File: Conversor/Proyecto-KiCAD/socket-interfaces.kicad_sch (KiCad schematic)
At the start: 37 parts

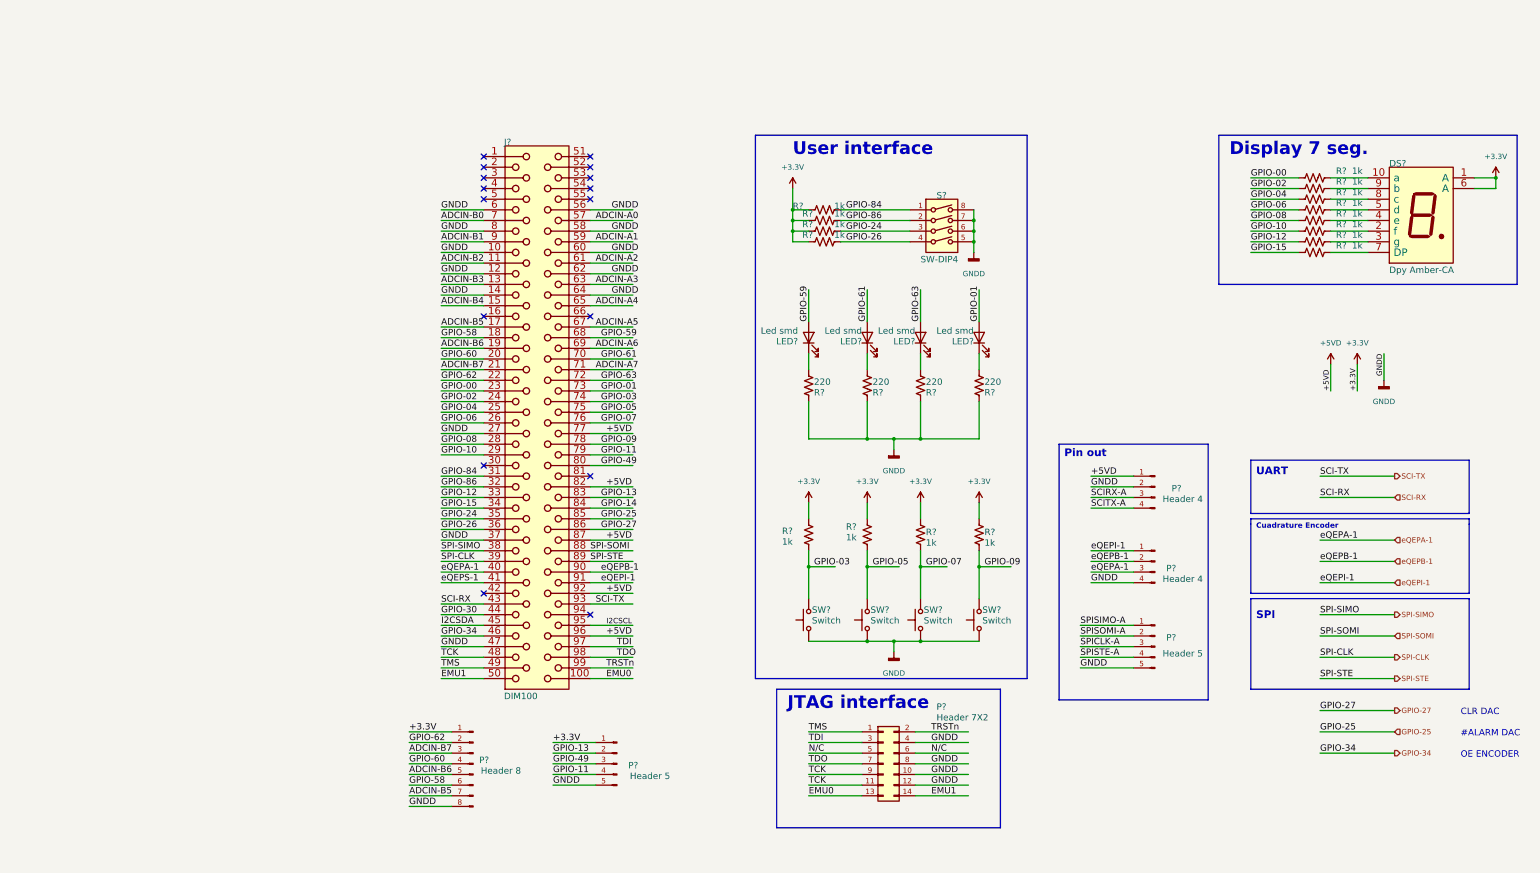
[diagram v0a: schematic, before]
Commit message: Seleccionar componentes de los que me dieron y seguir con la placa adaptadora
- OpAmp OPA365AID para acondicionamiento de señales del sensor de efecto
hall
- Los optos que hay son ACPL-P343 en vez de P480, que necesitan 15-30V
de alimentación. Preguntar si no es mejor cambiarlos por 6N137, de 5V de
Vcc
- Regulador solo hay LM7805 de 5Vout pero también necesito 3.3Vout
- No hay ningún diodo en las cosas que me dieron

Por hacer:
  - Preguntar por los 6N137 y algun regulador de 3V3 out
  - Preguntar por los diodos del puente del conversor
  - Terminar de pasar la placa adaptadora del DSP
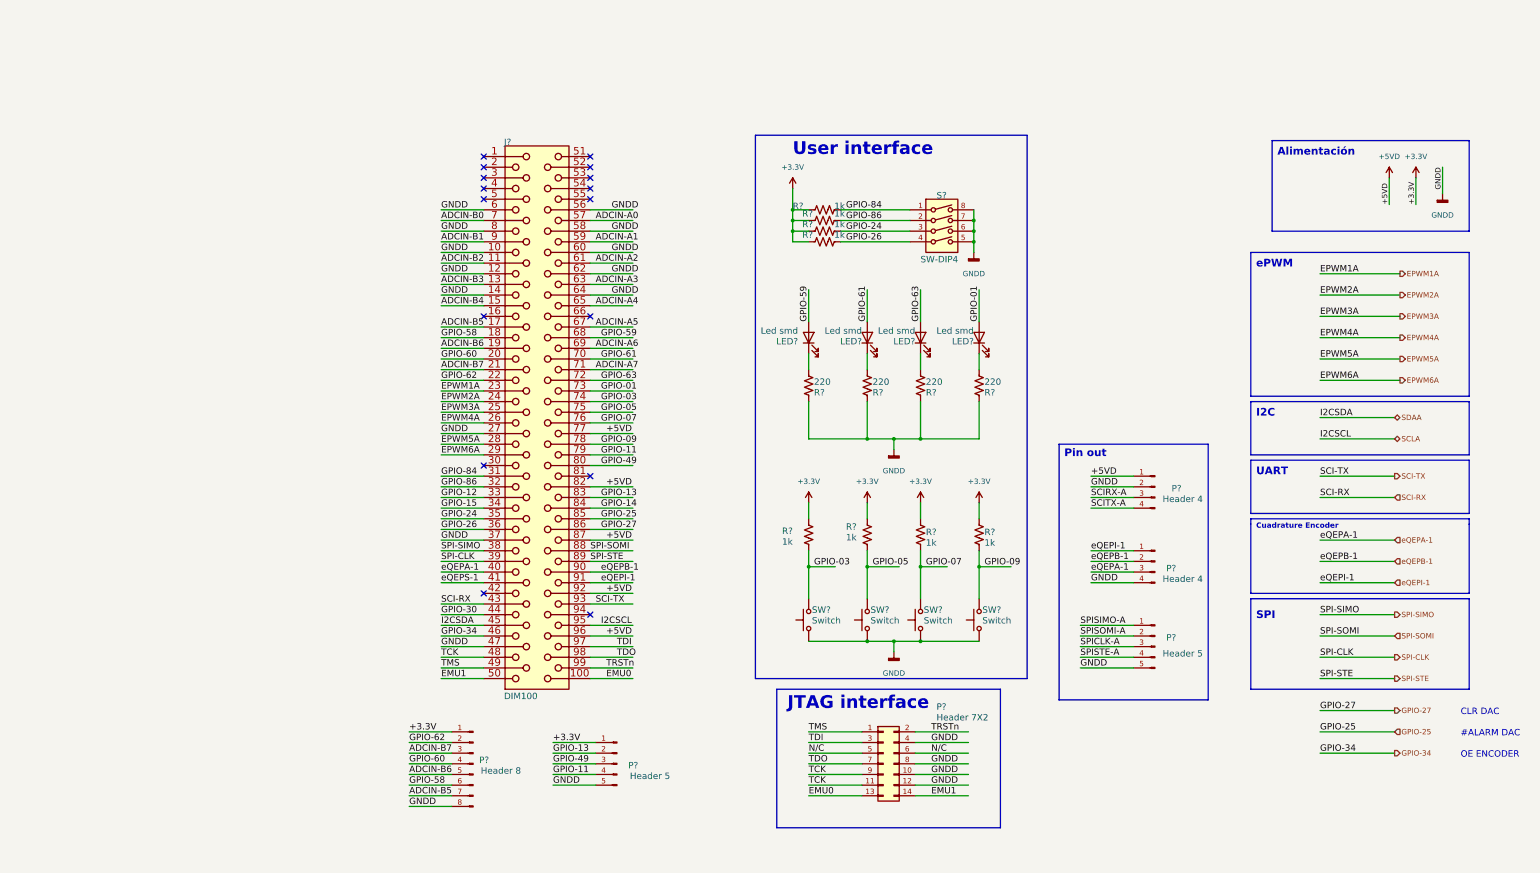
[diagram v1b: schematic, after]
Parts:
- removed DS?: Dpy Amber-CA, symbol dpy_amber-ca:Dpy_Amber-CA-
- removed R? (x8): 1k, symbol Device:R_US
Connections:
- net GPIO-00 renamed EPWM1A
- net GPIO-02 renamed EPWM2A
- net GPIO-04 renamed EPWM3A
- net GPIO-06 renamed EPWM4A
- net GPIO-08 renamed EPWM5A
- net GPIO-10 renamed EPWM6A
- net I2CSCL renamed SCLA
- net I2CSDA renamed SDAA
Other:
- note added: "Alimentación"
- note added: "I2C"
- note added: "ePWM"
- note removed: "Display 7 seg."

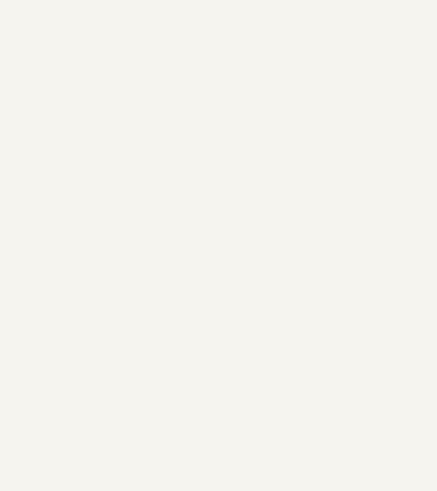
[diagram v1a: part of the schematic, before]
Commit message: Agregar simbolo, footprint y modelo 3D del slot DIMM100
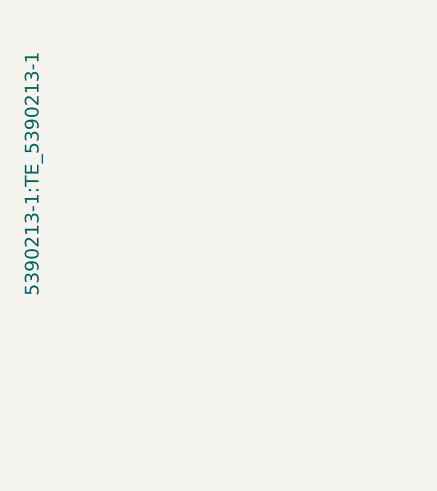
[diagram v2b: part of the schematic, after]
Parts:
- J?: footprint (none) -> 5390213-1:TE_5390213-1
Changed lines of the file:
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@@
       (effects (font (size 1.524 1.524)) (justify left bottom))
     )
-    (property "Footprint" "" (id 2) (at -78.74 2.286 0)
+    (property "Footprint" "5390213-1:TE_5390213-1" (id 2) (at -78.74 2.286 0)
       (effects (font (size 1.524 1.524)))
     )

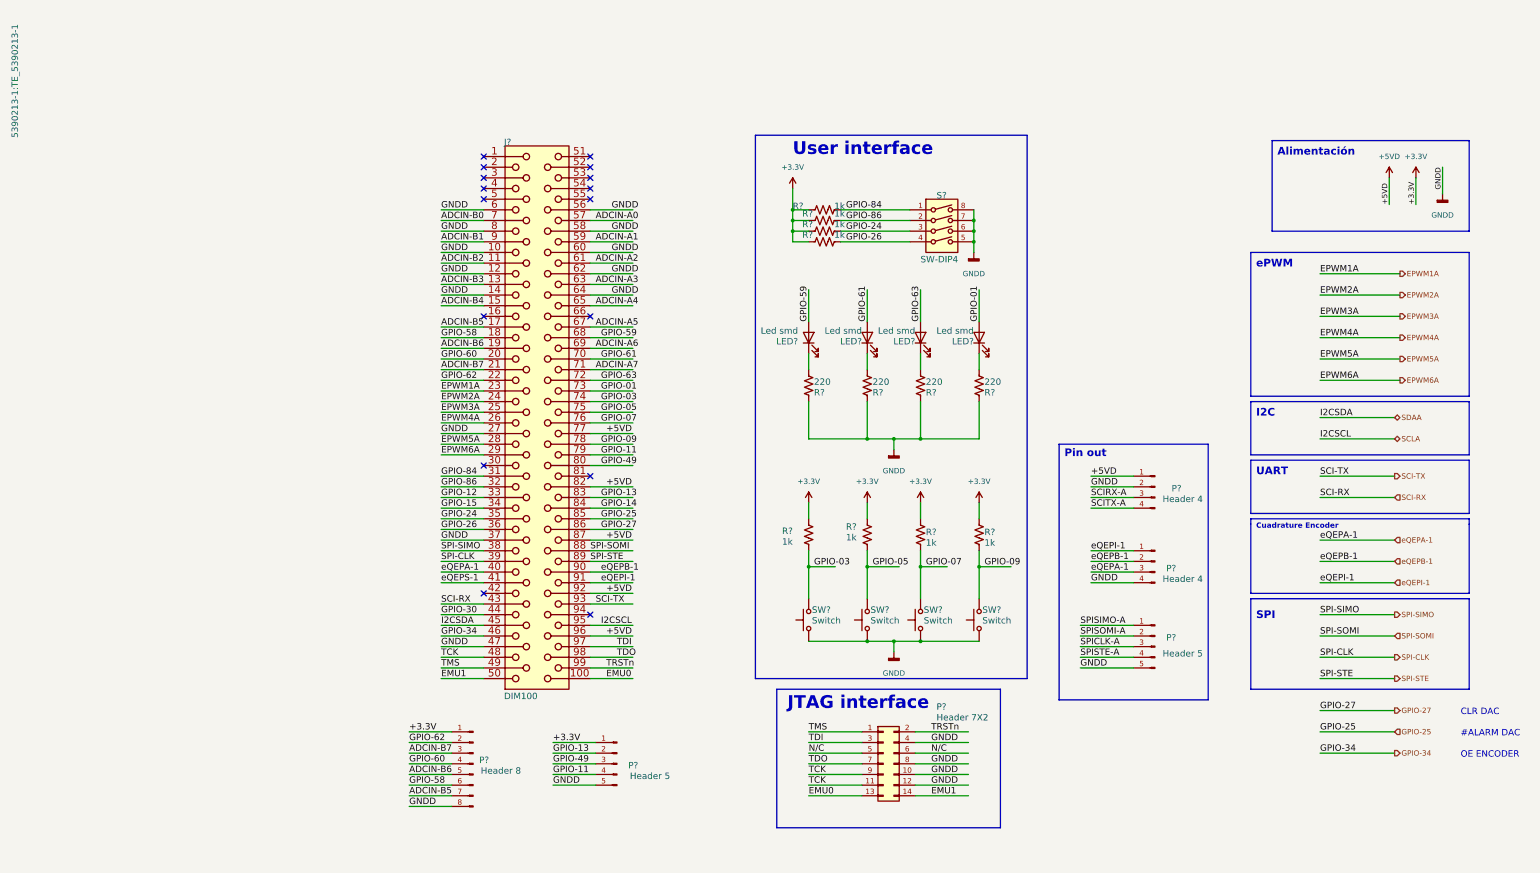
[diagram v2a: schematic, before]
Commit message: Continuar el paso de la placa adaptadora al proyecto
- El bloque de encoder y DAC se eliminan, no son necesarios
- Hay que agregar un selector entre 5V externo y por USB para el DSP, y ver como compatibilizarlo con la alimentación general
- Para el regulador de 3.3V se usa el mismo integrado que en la placa adaptadora (TI LP2985-3.3)
- Los optos son los ACPL-P480 en vez de los P343
Por hacer:
  - Terminar la placa adaptadora (USB-UART, Power Supply e I2C)
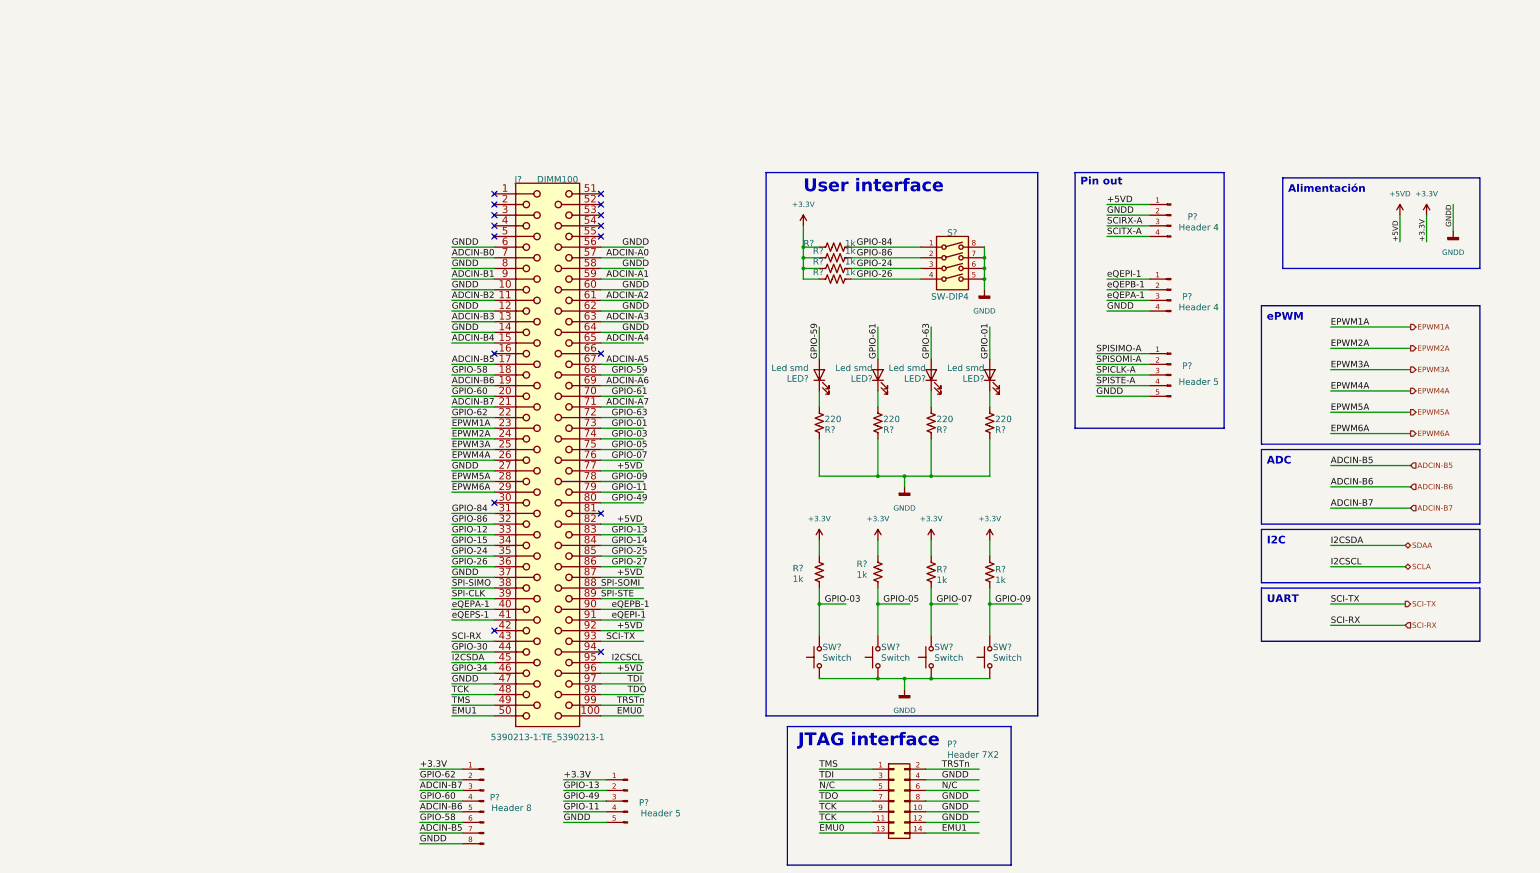
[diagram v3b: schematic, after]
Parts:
- J?: value DIM100 -> DIMM100
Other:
- note added: "ADC"
- note removed: "#ALARM DAC"
- note removed: "CLR DAC"
- note removed: "Cuadrature Encoder"
- note removed: "OE ENCODER"
- note removed: "SPI"
- moved on the sheet: J?, LED?, P?, R?, S?, SW?

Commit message: Terminar (casi) el traspaso de la placa adaptadora al proyecto
- Queda el selector entre 5V USB y 5V extern, pero todo esta en la hoja
de alimetación general, no dentro de la hoja del DSP
- Cambiar un poco los headers para poder testear (separado en Headers
5V, PWM, ADC, UART, I2C y GPIO)
- Agregar la hoja de datos del LP2985-3.3 (regulador de +3V3)
Por hacer:
  - Ver el tema de la asilacion de las lineas de datos I2C del LM5056,
porque tiene que unirse a una sola linea de datos bidireccional a la
salida del aislador (estan separadas para facilitar la aislación)
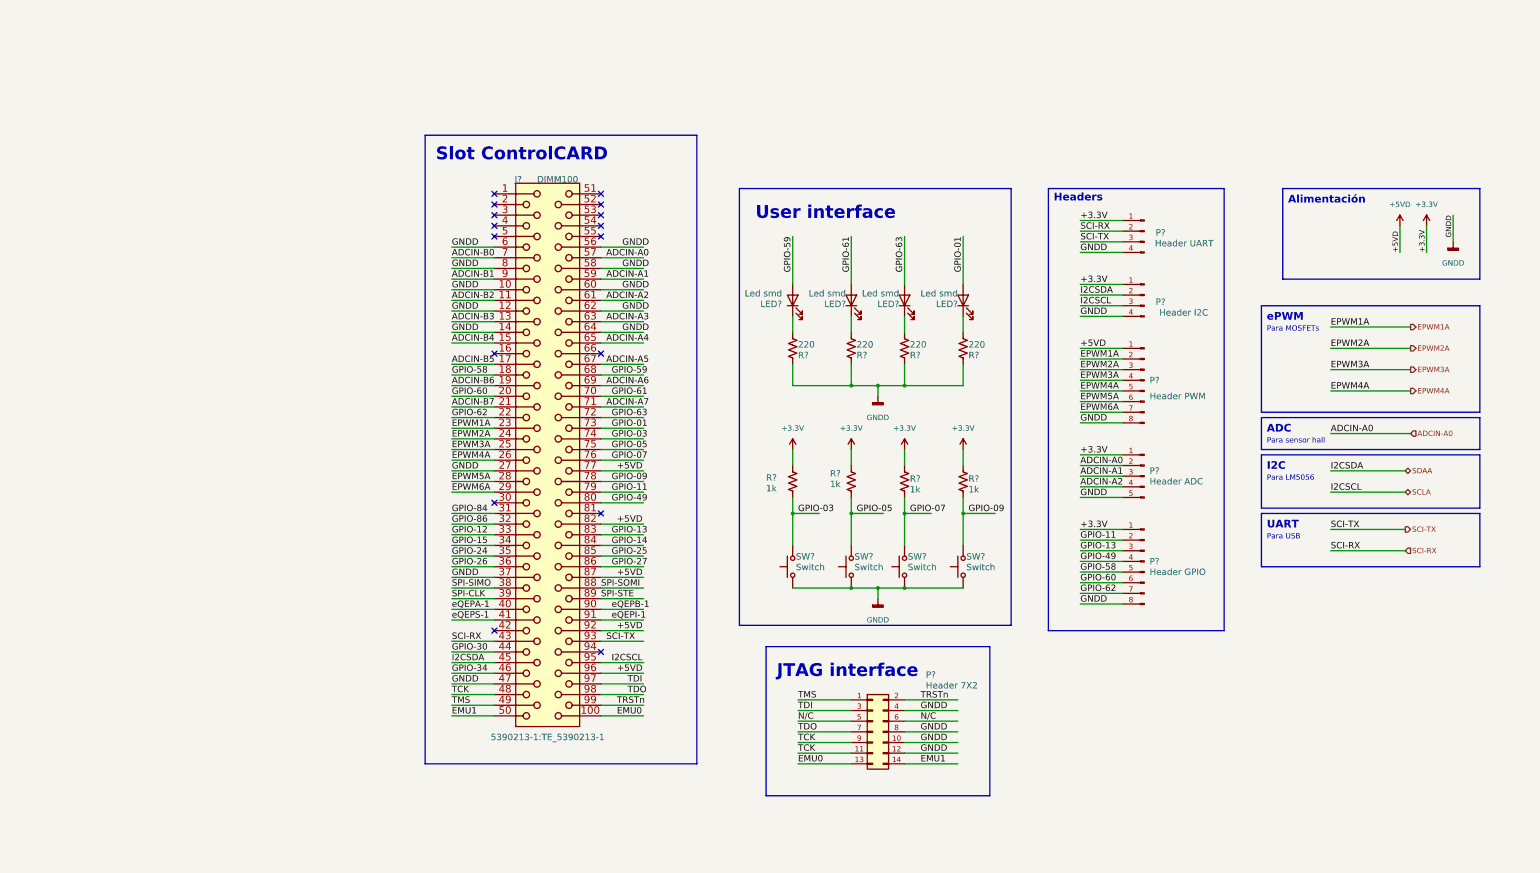
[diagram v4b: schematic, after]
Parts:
- removed P?: Header 8, symbol Connector:Conn_01x08_Male
- removed P? (x2): Header 5, symbol Connector:Conn_01x05_Male
- removed R? (x4): 1k, symbol Device:R_US
- removed S?: SW-DIP4, symbol Switch:SW_DIP_x04
- added P?: Header ADC, symbol Connector:Conn_01x05_Male
- added P?: Header GPIO, symbol Connector:Conn_01x08_Male
- added P?: Header PWM, symbol Connector:Conn_01x08_Male
- P?: value Header 4 -> Header UART
- P?: value Header 4 -> Header I2C
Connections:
- net SCIRX-A is gone; now on net SCI-TX: P?.3 (Pin_3)
- net SCITX-A is gone; now on net GNDD: P?.4 (Pin_4)
- net +3V3: now also P?.1 (Pin_1), P?.1 (Pin_1), P?.1 (Pin_1), P?.1 (Pin_1)
- net +5VD: now also P?.1 (Pin_1); no longer P?.1 (Pin_1)
- net ADCIN-A0: now also P?.2 (Pin_2)
- net ADCIN-A1: now also P?.3 (Pin_3)
- net ADCIN-A2: now also P?.4 (Pin_4)
- net EPWM1A: now also P?.2 (Pin_2)
- net EPWM2A: now also P?.3 (Pin_3)
- net EPWM3A: now also P?.4 (Pin_4)
- net EPWM4A: now also P?.5 (Pin_5)
- net EPWM5A: now also P?.6 (Pin_6)
- net EPWM6A: now also P?.7 (Pin_7)
- net GNDD: now also P?.5 (Pin_5), P?.8 (Pin_8), P?.8 (Pin_8); no longer P?.2 (Pin_2)
- net GPIO-11: now also P?.2 (Pin_2)
- net GPIO-13: now also P?.3 (Pin_3)
- net GPIO-49: now also P?.4 (Pin_4)
- net GPIO-58: now also P?.5 (Pin_5)
- net GPIO-60: now also P?.6 (Pin_6)
- net GPIO-62: now also P?.7 (Pin_7)
- net SCI-RX: now also P?.2 (Pin_2)
- net SCLA: now also P?.3 (Pin_3)
- net SDAA: now also P?.2 (Pin_2)
- net eQEPA-1: no longer P?.3 (Pin_3)
- net eQEPB-1: no longer P?.2 (Pin_2)
- net eQEPI-1: no longer P?.1 (Pin_1)
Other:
- note added: "Headers"
- note added: "Para LM5056"
- note added: "Para MOSFETs"
- note added: "Para USB"
- note added: "Para sensor hall"
- note added: "Slot ControlCARD"
- note removed: "Pin out"
- moved on the sheet: LED?, P?, R?, SW?
